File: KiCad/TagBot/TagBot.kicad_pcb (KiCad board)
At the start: 4 copper layers, 54 x 57 mm, 81 parts, among them IC101 ADXL343BCCZ-RL, J1001 Conn_01x06, J1002 Conn_01x06, J101 Conn_ST_STDC14, J103 Conn_01x03, J105 Conn_01x02, J1101 Conn_01x04, J801 Conn_01x06, J901 Conn_01x08, SW701 SW_Push, SW702 SW_Push, U101 STM32G431CBUx, U201 ZXBM5210-SP, U301 ZXBM5210-SP, U401 MP1475S, U501 BU33SD5WG-TR, Y101 Crystal

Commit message: upadate pcb name
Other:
- board text added: "16/10/2024 Projet TagBot"
- board text added: "M. CARONELLO L. CHAPART C. FRICOT"

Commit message: update routage
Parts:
- removed C101, C102: 1u, Capacitor_SMD:C_0402_1005Metric
- removed IC101: ADXL343BCCZ-RL, ADXL343BCCZ-RL:ADXL343BCCZRL
- added C1: 1u, Capacitor_SMD:C_0603_1608Metric, F.Cu at (95.5, 76.6)
- added C2: 1u, Capacitor_SMD:C_0603_1608Metric, F.Cu at (95.5, 79.2)
- added TP1: TestPoint, TestPoint:TestPoint_Pad_D1.5mm, F.Cu at (67.2, 55.4)
- added TP2: TestPoint, TestPoint:TestPoint_Pad_D1.5mm, F.Cu at (65.0, 52.1)
- added TP3: TestPoint, TestPoint:TestPoint_Pad_D1.5mm, F.Cu at (69.8, 54.1)
- added TP4: TestPoint, TestPoint:TestPoint_Pad_D1.5mm, F.Cu at (76.1, 55.9)
- added U1: ADXL343, Package_LGA:LGA-14_3x5mm_P0.8mm_LayoutBorder1x6y, F.Cu at (68.1, 72.2)
- C103, C108, C111, C201, C202, C301, C302, C501, C502: footprint Capacitor_SMD:C_0402_1005Metric -> Capacitor_SMD:C_0603_1608Metric
- moved C301 3.28 mm to (69.3, 51.7)
- moved C302 3.16 mm to (69.3, 50.2)
- moved U301 2.18 mm to (74.3, 50.8), turned to 0 degrees
- moved C201 1.51 mm to (54.5, 51.5)
- moved U201 1.41 mm to (59.5, 50.9), turned to 0 degrees
- moved C202 1.29 mm to (54.5, 50.0)
- moved R804 0.70 mm to (74.2, 73.2)
- moved C103 0.55 mm to (61.8, 57.5)
- moved D603 0.35 mm to (50.9, 54.4)
- moved R603 0.35 mm to (54.0, 54.4)
- moved L101 0.34 mm to (74.2, 68.8)
- moved C108 0.32 mm to (74.5, 71.2)
- moved C111 0.32 mm to (76.0, 71.2)
- moved C501 0.26 mm to (56.5, 67.8)
- moved C106 0.25 mm to (63.5, 56.1)
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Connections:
- J1001 pad 1: /RIGHT_OUT1 -> /RIGHT_OUT2
- J1001 pad 6: /RIGHT_OUT2 -> /RIGHT_OUT1
- J1002 pad 1: /LEFT_OUT1 -> /LEFT_OUT2
- J1002 pad 6: /LEFT_OUT2 -> /LEFT_OUT1
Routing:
- net /RIGHT_OUT2: track 32.6 -> 8.88 mm
- net /Valim: track 38.0 -> 56.1 mm, vias 4 -> 2
- net /LEFT_OUT2: track 21.2 -> 12.2 mm
- net +3.3V: track 78.9 -> 70.0 mm, vias 10 -> 9
- net /LEFT_OUT1: track 5.28 -> 11.8 mm
- net /RIGHT_FWD: track 19.7 -> 14.7 mm
- net /RIGHT_REV: track 8.94 -> 13.9 mm
- net /RIGHT_OUT1: track 4.32 -> 7.92 mm
- net /LEFT_REV: track 18.2 -> 15.3 mm
- net /OLED_SDA: track 26.1 -> 23.7 mm
- net /Encoder_Left_B: track 22.0 -> 23.9 mm
- net /STLINK_TX: track 25.5 -> 26.7 mm
- net /LEFT_FWD: track 23.6 -> 22.6 mm
- net /Encoder_Right_B: track 13.6 -> 14.5 mm, vias 0 -> 1
- net /Interrupt2: track 13.1 -> 12.4 mm
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
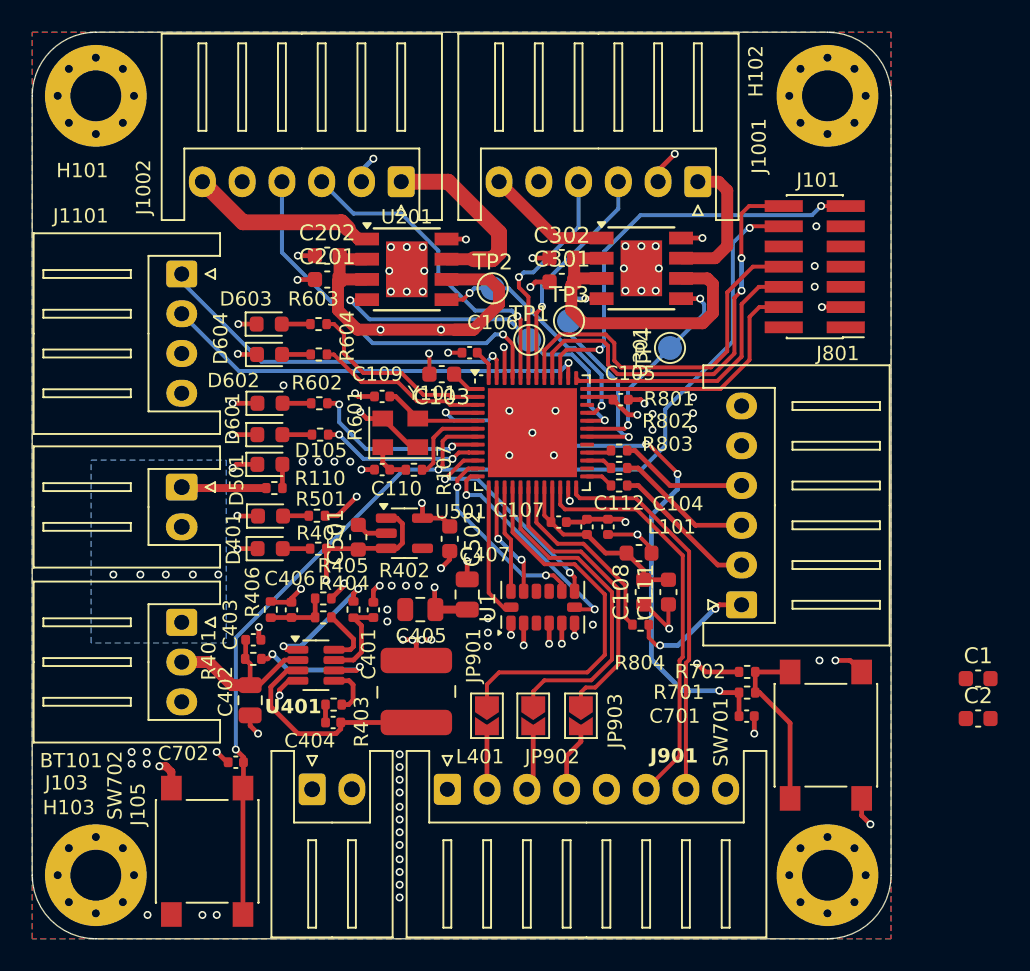
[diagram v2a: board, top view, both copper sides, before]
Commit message: correction routage
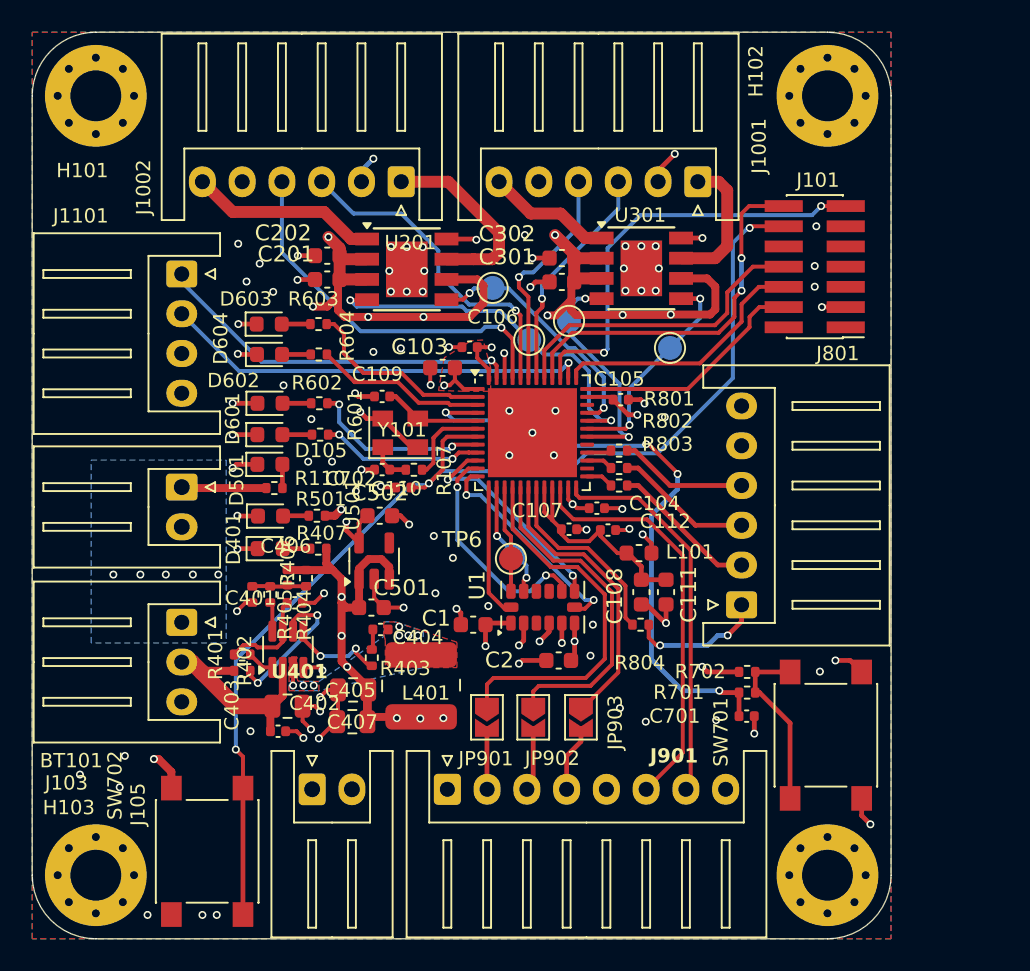
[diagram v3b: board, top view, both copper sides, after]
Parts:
- added TP5: TestPoint, TestPoint:TestPoint_Pad_D1.5mm, B.Cu at (66.3, 68.9)
- added TP6: TestPoint, TestPoint:TestPoint_Pad_D1.5mm, F.Cu at (66.1, 69.1)
- moved C1 31.9 mm to (63.7, 73.2)
- moved C2 26.6 mm to (69.1, 75.5)
- moved C702 20.2 mm to (59.3, 64.6)
- moved C407 10.8 mm to (56.1, 79.3), turned to 180 degrees
- moved R402 7.55 mm to (49.2, 75.1), turned to 0 degrees
- moved C405 6.58 mm to (56.2, 77.3)
- moved C404 6.57 mm to (57.9, 73.5)
- moved C403 5.96 mm to (51.5, 80.0)
- moved C401 4.96 mm to (52.5, 71.9), turned to 0 degrees
- moved C502 4.63 mm to (57.9, 66.4), turned to 0 degrees
- moved C501 4.50 mm to (57.3, 72.2), turned to 0 degrees
- moved R405 4.47 mm to (49.8, 71.3), turned to -90 degrees
- moved L401 4.26 mm to (60.5, 75.2), turned to -90 degrees
- moved R403 3.80 mm to (57.4, 75.3), turned to 90 degrees
- moved R404 3.63 mm to (51.0, 71.3), turned to 90 degrees
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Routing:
- net Net-(U401-SW): track 13.7 -> 1.14 mm, vias 0 -> 7
- net GND: track 64.4 -> 73.1 mm, vias 107 -> 105
- net +5V: track 18.4 -> 26.8 mm, vias 7 -> 6
- net Net-(U401-PG): track 8.10 -> 1.73 mm, vias 2 -> 0
- net +3.3V: track 70.0 -> 75.0 mm, vias 9 -> 11
- net /Valim: track 56.1 -> 60.4 mm, vias 2 -> 8
- net /STLINK_RX: track 27.3 -> 23.5 mm
- net /SYS_JTDO-SWO: track 23.5 -> 19.7 mm
- net Net-(U401-BST): track 3.11 -> 5.93 mm, vias 0 -> 2
- net /Interrupt2: track 12.4 -> 14.4 mm
- net Net-(U401-FB): track 3.74 -> 2.04 mm
- net /NRST: track 72.0 -> 73.5 mm
- net /SYS_JTMS-SWDIO: track 16.1 -> 14.9 mm
- net /SYS_JTCK-SWCLK: track 17.5 -> 16.4 mm
- net /LEFT_FWD: track 22.6 -> 23.5 mm
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- added copper zone on F.Cu, net +3.3V
- added copper zone on B.Cu, net Net-(U401-SW)
- added copper zone on F.Cu, net Net-(U401-SW)

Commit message: update silkscreen
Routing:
- net GND: track 73.1 -> 70.7 mm, vias 105 -> 113
- net /Encoder_Right_A: track 15.5 -> 15.0 mm

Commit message: update antenne
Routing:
- net GND: track 70.7 -> 71.4 mm, vias 113 -> 151

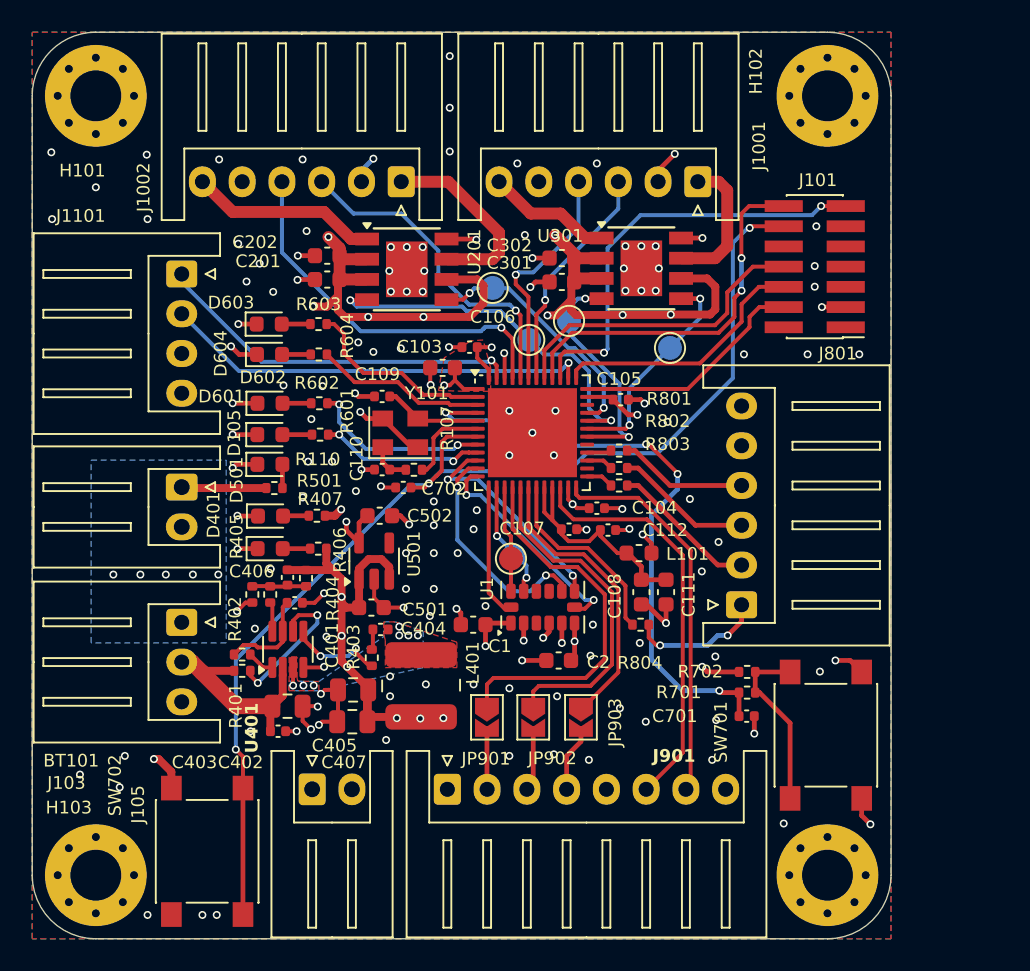
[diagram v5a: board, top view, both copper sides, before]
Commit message: fixed switch footprint and genrated gerber files
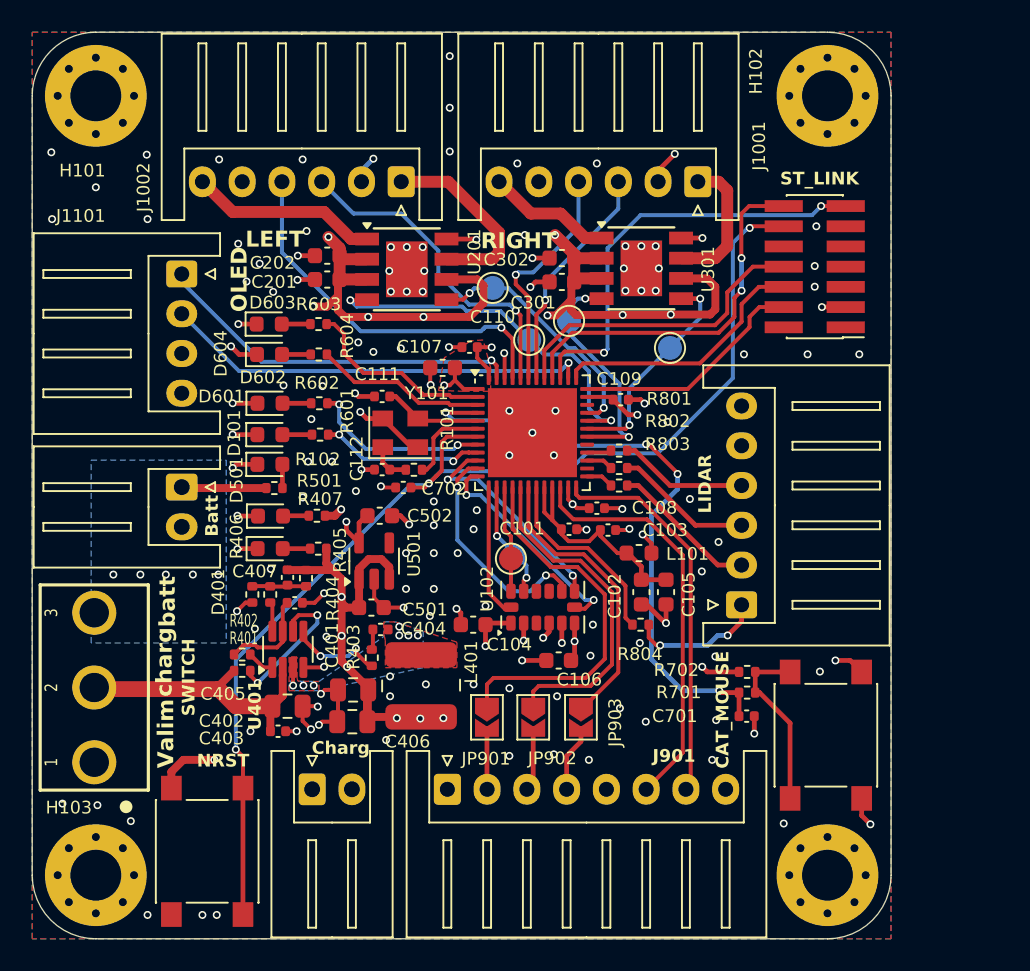
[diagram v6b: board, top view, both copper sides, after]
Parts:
- removed J103: Conn_01x03, Connector_JST:JST_XH_S3B-XH-A_1x03_P2.50mm_Horizontal
- added charg: switch, wurth_472121020311:472121020311, F.Cu at (39.9, 77.2)
- renumbered BT101 to Batt, C107 to C101, C108 to C102, C112 to C103, C1 to C104, C111 to C105, C2 to C106, C103 to C107, C104 to C108, C105 to C109, C106 to C110, C109 to C111, C110 to C112, C407 to C406, C406 to C407, SW701 to CAT_MOUSE, J105 to Charg, D105 to D101, TP2 to LEFT_REV, J801 to LIDAR, TP5 to MISO, TP6 to MOSI101, SW702 to NRST, R107 to R101, R110 to R102, R406 to R405, R405 to R406, TP3 to RIGHT_FWD, TP4 to RIGHT_REV, J101 to ST_LINK, TP1 to TPLEFT_FWD, U1 to U102
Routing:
- net /Valim: track 60.4 -> 64.7 mm
- net Net-(J101-Pin_1): track 12.5 -> 14.4 mm
- net GND: track 71.4 -> 72.9 mm
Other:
- board text added: "22/10/2024 Projet TagBot"
- board text added: "LEFT"
- board text added: "OLED"
- board text added: "RIGHT"
- board text added: "SWITCH"
- board text added: "Valim"
- board text added: "batt"
- board text removed: "16/10/2024 Projet TagBot"
